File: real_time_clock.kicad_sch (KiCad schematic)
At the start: 5 parts, among them U8 DS3231M

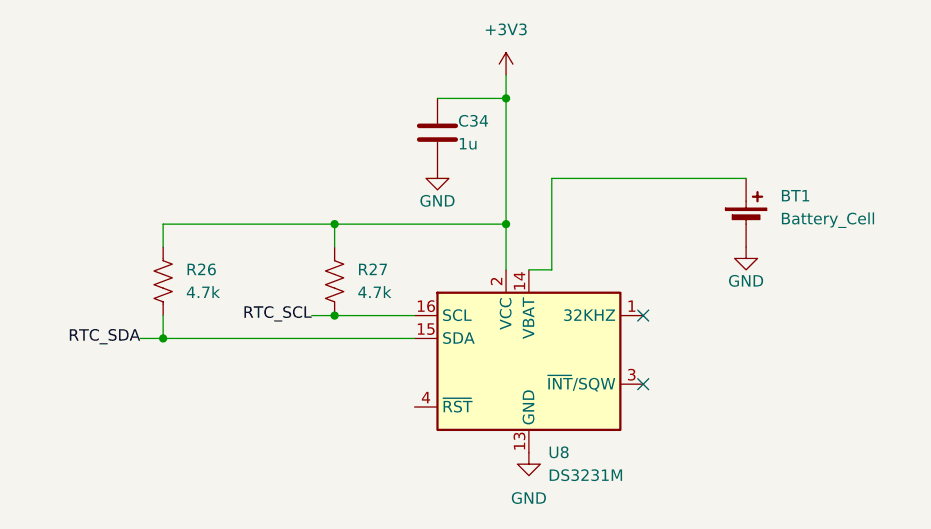
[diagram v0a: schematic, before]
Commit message: Add nixie tube net labels and dc/dc converter
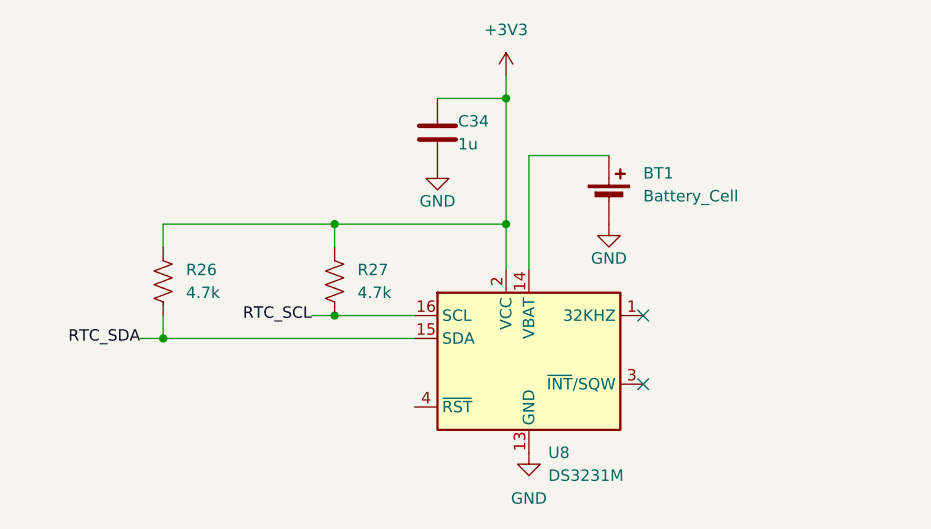
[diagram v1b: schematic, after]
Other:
- moved on the sheet: BT1
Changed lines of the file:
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@@
 	(wire
 		(pts
-			(xy 156.21 96.52) (xy 156.21 86.36)
-		)
-		(stroke
-			(width 0)
-			(type default)
-		)
-	)
-	(wire
-		(pts
-			(xy 156.21 96.52) (xy 153.67 96.52)
+			(xy 153.67 96.52) (xy 153.67 83.82)
 		)
 		(stroke
@@
 	(wire
 		(pts
-			(xy 156.21 86.36) (xy 177.8 86.36)
+			(xy 153.67 83.82) (xy 162.56 83.82)
 		)
 		(stroke
@@
 	(symbol
 		(lib_id "Device:Battery_Cell")
-		(at 177.8 91.44 0)
+		(at 162.56 88.9 0)
 		(unit 1)
 		(exclude_from_sim no)
@@
 		(fields_autoplaced yes)
 		(property "Reference" "BT1"
-			(at 181.61 88.3284 0)
+			(at 166.37 85.7884 0)
 			(effects
 				(font
@@
 		)
 		(property "Value" "Battery_Cell"
-			(at 181.61 90.8684 0)
+			(at 166.37 88.3284 0)
 			(effects
 				(font
@@
 		)
 		(property "Footprint" "Battery:BatteryHolder_Keystone_500"
-			(at 177.8 89.916 90)
+			(at 162.56 87.376 90)
 			(effects
 				(font
@@
 		)
 		(property "Datasheet" "~"
-			(at 177.8 89.916 90)
+			(at 162.56 87.376 90)
 			(effects
 				(font
@@
 		)
 		(property "Description" "Single-cell battery"
-			(at 177.8 91.44 0)
+			(at 162.56 88.9 0)
 			(effects
 				(font
@@
 		)
 		(property "Sim.Device" "V"
-			(at 177.8 91.44 0)
+			(at 162.56 88.9 0)
 			(effects
 				(font
@@
 		)
 		(property "Sim.Type" "DC"
-			(at 177.8 91.44 0)
+			(at 162.56 88.9 0)
 			(effects
 				(font
@@
 		)
 		(property "Sim.Pins" "1=+ 2=-"
-			(at 177.8 91.44 0)
+			(at 162.56 88.9 0)
 			(effects
 				(font
@@
 	(symbol
 		(lib_id "power:GND")
-		(at 177.8 93.98 0)
+		(at 162.56 91.44 0)
 		(unit 1)
 		(exclude_from_sim no)
@@
 		(dnp no)
 		(property "Reference" "#PWR077"
-			(at 177.8 100.33 0)
+			(at 162.56 97.79 0)
 			(effects
 				(font
@@
 		)
 		(property "Value" "GND"
-			(at 177.8 97.79 0)
+			(at 162.56 95.25 0)
 			(effects
 				(font
@@
 		)
 		(property "Footprint" ""
-			(at 177.8 93.98 0)
+			(at 162.56 91.44 0)
 			(effects
 				(font
@@
 		)
 		(property "Datasheet" ""
-			(at 177.8 93.98 0)
+			(at 162.56 91.44 0)
 			(effects
 				(font
@@
 		)
 		(property "Description" "Power symbol creates a global label with name \"GND\" , ground"
-			(at 177.8 93.98 0)
-			(effects
-				(font
+			(at 162.56 91.44 0)
+			(effects
+				(font

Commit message: Update power supply layout and add associated components
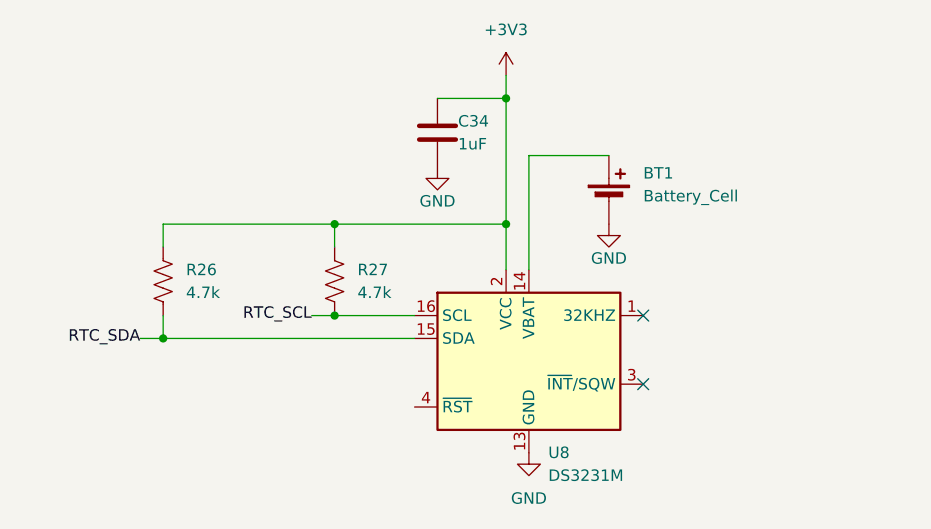
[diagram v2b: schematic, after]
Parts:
- BT1: footprint Battery:BatteryHolder_Keystone_500 -> Battery:BatteryHolder_Keystone_3034_1x20mm
- C34: value 1u -> 1uF
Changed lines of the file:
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@@
 			)
 		)
-		(property "Footprint" "Battery:BatteryHolder_Keystone_500"
+		(property "Footprint" "Battery:BatteryHolder_Keystone_3034_1x20mm"
 			(at 162.56 87.376 90)
 			(effects
@@
 			)
 		)
-		(property "Value" "1u"
+		(property "Value" "1uF"
 			(at 145.796 82.55 0)
 			(effects

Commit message: Add global labels for nets spanning several sheets
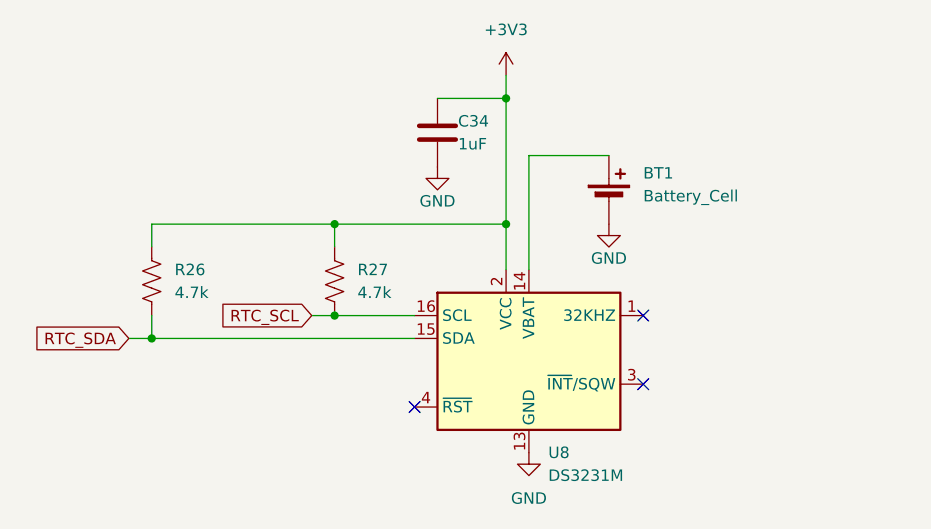
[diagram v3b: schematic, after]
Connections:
- no-connect marks 2 -> 3
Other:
- moved on the sheet: R26
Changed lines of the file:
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@@
 	(paper "A4")
-	(junction
-		(at 113.03 104.14)
-		(diameter 0)
-		(color 0 0 0 0)
-	)
 	(junction
 		(at 151.13 77.47)
@@
 	)
 	(junction
+		(at 111.76 104.14)
+		(diameter 0)
+		(color 0 0 0 0)
+	)
+	(junction
 		(at 151.13 91.44)
 		(diameter 0)
@@
 	)
 	(no_connect
+		(at 140.97 111.76)
+	)
+	(no_connect
 		(at 166.37 109.22)
 	)
@@
 	(wire
 		(pts
-			(xy 113.03 93.98) (xy 113.03 91.44)
+			(xy 111.76 93.98) (xy 111.76 91.44)
 		)
 		(stroke
@@
 	(wire
 		(pts
-			(xy 113.03 91.44) (xy 132.08 91.44)
+			(xy 111.76 91.44) (xy 132.08 91.44)
 		)
 		(stroke
@@
 	(wire
 		(pts
-			(xy 140.97 104.14) (xy 113.03 104.14)
-		)
-		(stroke
-			(width 0)
-			(type default)
-		)
-	)
-	(wire
-		(pts
 			(xy 151.13 77.47) (xy 151.13 91.44)
 		)
@@
 	(wire
 		(pts
+			(xy 111.76 104.14) (xy 140.97 104.14)
+		)
+		(stroke
+			(width 0)
+			(type default)
+		)
+	)
+	(wire
+		(pts
 			(xy 151.13 91.44) (xy 151.13 96.52)
 		)
@@
 	(wire
 		(pts
-			(xy 113.03 101.6) (xy 113.03 104.14)
+			(xy 111.76 101.6) (xy 111.76 104.14)
 		)
 		(stroke
@@
 	(wire
 		(pts
-			(xy 110.49 104.14) (xy 113.03 104.14)
-		)
-		(stroke
-			(width 0)
-			(type default)
-		)
-	)
-	(label "RTC_SCL"
-		(at 129.54 101.6 180)
+			(xy 109.22 104.14) (xy 111.76 104.14)
+		)
+		(stroke
+			(width 0)
+			(type default)
+		)
+	)
+	(global_label "RTC_SDA"
+		(shape input)
+		(at 109.22 104.14 180)
+		(fields_autoplaced yes)
 		(effects
 			(font
@@
 			(justify right)
 		)
-	)
-	(label "RTC_SDA"
-		(at 110.49 104.14 180)
+		(property "Intersheetrefs" "${INTERSHEET_REFS}"
+			(at 98.1915 104.14 0)
+			(effects
+				(font
+					(size 1.27 1.27)
+				)
+				(justify right)
+				(hide yes)
+			)
+		)
+	)
+	(global_label "RTC_SCL"
+		(shape input)
+		(at 129.54 101.6 180)
+		(fields_autoplaced yes)
 		(effects
 			(font
@@
 			)
 			(justify right)
+		)
+		(property "Intersheetrefs" "${INTERSHEET_REFS}"
+			(at 118.572 101.6 0)
+			(effects
+				(font
+					(size 1.27 1.27)
+				)
+				(justify right)
+				(hide yes)
+			)
 		)
 	)
@@
 	(symbol
 		(lib_id "Device:R_US")
-		(at 113.03 97.79 0)
+		(at 111.76 97.79 0)
 		(unit 1)
 		(exclude_from_sim no)
@@
 		(fields_autoplaced yes)
 		(property "Reference" "R26"
-			(at 115.57 96.5199 0)
+			(at 114.3 96.5199 0)
 			(effects
 				(font
@@
 		)
 		(property "Value" "4.7k"
-			(at 115.57 99.0599 0)
+			(at 114.3 99.0599 0)
 			(effects
 				(font
@@
 		)
 		(property "Footprint" "Resistor_SMD:R_0603_1608Metric"
-			(at 114.046 98.044 90)
+			(at 112.776 98.044 90)
 			(effects
 				(font
@@
 		)
 		(property "Datasheet" "~"
-			(at 113.03 97.79 0)
+			(at 111.76 97.79 0)
 			(effects
 				(font
@@
 		)
 		(property "Description" "Resistor, US symbol"
-			(at 113.03 97.79 0)
-			(effects
-				(font
+			(at 111.76 97.79 0)
+			(effects
+				(font

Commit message: Add DigiKey part numbers to components
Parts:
- C34: DigikeyPN (none) -> 1276-1184-1-ND
- R26, R27: DigikeyPN (none) -> 311-4.70KHRCT-ND
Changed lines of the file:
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@@
+			)
+		)
+		(property "DigiKeyPN" ""
+			(at 153.67 106.68 0)
+			(effects
+				(font
+					(size 1.27 1.27)
+				)
+				(hide yes)
 			)
 		)
@@
 			)
 		)
+		(property "DigiKeyPN" ""
+			(at 162.56 88.9 0)
+			(effects
+				(font
+					(size 1.27 1.27)
+				)
+				(hide yes)
+			)
+		)
 		(pin "1"
 		)
@@
 			)
 		)
+		(property "DigikeyPN" "1276-1184-1-ND"
+			(at 143.51 81.28 0)
+			(effects
+				(font
+					(size 1.27 1.27)
+				)
+				(hide yes)
+			)
+		)
+		(property "DigiKeyPN" ""
+			(at 143.51 81.28 0)
+			(effects
+				(font
+					(size 1.27 1.27)
+				)
+				(hide yes)
+			)
+		)
 		(pin "1"
 		)
@@
 			)
 		)
+		(property "DigiKeyPN" ""
+			(at 132.08 97.79 0)
+			(effects
+				(font
+					(size 1.27 1.27)
+				)
+				(hide yes)
+			)
+		)
+		(property "DigikeyPN" "311-4.70KHRCT-ND"
+			(at 132.08 97.79 0)
+			(effects
+				(font
+					(size 1.27 1.27)
+				)
+				(hide yes)
+			)
+		)
 		(pin "1"
 		)
@@
 			(at 111.76 97.79 0)
 			(effects
+				(font
+					(size 1.27 1.27)
+				)
+				(hide yes)
+			)
+		)
+		(property "DigiKeyPN" ""
+			(at 111.76 97.79 0)
+			(effects
+				(font
+					(size 1.27 1.27)
+				)
+				(hide yes)
+			)
+		)
+		(property "DigikeyPN" "311-4.70KHRCT-ND"
+			(at 111.76 97.79 0)
+			(effects

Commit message: BOM simplification of redundant components
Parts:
- BT1: DigikeyPN (none) -> 36-3034-ND; LCSCPN (none) -> C5199422; MFN (none) -> Keystone Electronics; MPN (none) -> 3034
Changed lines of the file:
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@@
+			)
+		)
+		(property "Sim.Type" ""
+			(at 153.67 106.68 0)
+			(effects
+				(font
+					(size 1.27 1.27)
+				)
+				(hide yes)
 			)
 		)
@@
 			)
 		)
-		(property "Sim.Device" "V"
+		(property "MFN" "Keystone Electronics"
 			(at 162.56 88.9 0)
 			(effects
@@
 			)
 		)
-		(property "Sim.Type" "DC"
+		(property "MPN" "3034"
 			(at 162.56 88.9 0)
 			(effects
@@
 			)
 		)
-		(property "Sim.Pins" "1=+ 2=-"
+		(property "DigikeyPN" "36-3034-ND"
 			(at 162.56 88.9 0)
 			(effects
@@
 			)
 		)
-		(property "DigiKeyPN" ""
+		(property "LCSCPN" "C5199422"
 			(at 162.56 88.9 0)
 			(effects
@@
 			)
 		)
+		(property "Sim.Type" ""
+			(at 143.51 81.28 0)
+			(effects
+				(font
+					(size 1.27 1.27)
+				)
+				(hide yes)
+			)
+		)
 		(pin "1"
 		)
@@
 			)
 		)
+		(property "Sim.Type" ""
+			(at 132.08 97.79 0)
+			(effects
+				(font
+					(size 1.27 1.27)
+				)
+				(hide yes)
+			)
+		)
 		(pin "1"
 		)
@@
 			(at 111.76 97.79 0)
 			(effects
+				(font
+					(size 1.27 1.27)
+				)
+				(hide yes)
+			)
+		)
+		(property "Sim.Type" ""
+			(at 111.76 97.79 0)
+			(effects
